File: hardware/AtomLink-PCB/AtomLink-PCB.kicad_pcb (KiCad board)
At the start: 2 copper layers, 21 x 21 mm, 22 parts, among them J1 Conn_01x03, J2 Atom1, J3 Atom2, J4 PF cable, Q1 AS2309, Q2 MUN5235, Q3 AS2309, Q4 MUN5235, U1 LMZM23600V5

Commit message: Schematic & layout changes
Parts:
- added D2: PSM712, Package_TO_SOT_SMD:SOT-23, F.Cu at (47.0, 31.8)
- added Q5: MUN5235, Package_TO_SOT_SMD:SOT-323_SC-70, F.Cu at (45.8, 25.5)
- added R10: ?, Resistor_SMD:R_0402_1005Metric, F.Cu at (45.8, 22.9)
- added R7: 2.2k, Resistor_SMD:R_0805_2012Metric, F.Cu at (49.3, 23.2)
- added R9: 100, Resistor_SMD:R_0402_1005Metric, F.Cu at (45.8, 21.6)
- J4: footprint Connector_PinHeader_2.00mm:PinHeader_1x04_P2.00mm_Vertical -> Connector_PinHeader_1.27mm:PinHeader_1x04_P1.27mm_Vertical
- moved R5 40.8 mm to (62.9, 26.8)
- moved R6 39.6 mm to (61.0, 29.9)
- moved Q2 35.5 mm to (54.5, 33.9)
- moved C2 34.2 mm to (50.4, 34.0)
- moved U1 33.7 mm to (53.1, 19.2), turned to -90 degrees
- moved Q3 33.4 mm to (64.1, 37.4)
- moved R2 33.4 mm to (64.8, 34.5)
- moved R3 33.4 mm to (63.7, 34.5)
- moved R4 33.4 mm to (58.9, 34.6)
- moved R8 33.4 mm to (57.8, 34.6)
- moved D1 32.7 mm to (58.6, 22.3)
- moved C1 32.5 mm to (51.5, 26.6)
- moved Q1 30.9 mm to (55.6, 30.2)
- moved R7 29.1 mm to (53.3, 22.9)
- moved C3 27.0 mm to (48.6, 20.0), turned to 180 degrees
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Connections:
- J1 pad 1: unconnected-(J1-Pad1) -> Net-(J1-Pad1)
- J1 pad 2: unconnected-(J1-Pad2) -> +5V
- J1 pad 3: unconnected-(J1-Pad3) -> GND
- J2 pad 3: G25_ADC -> G25
- J3 pad 1: G33 -> G33_ADC
- Q2 pad 3: G23 -> G21
- Q4 pad 3: G33 -> G25
- R4 pad 2: G25_ADC -> G33_ADC
- R8 pad 1: G25_ADC -> G33_ADC

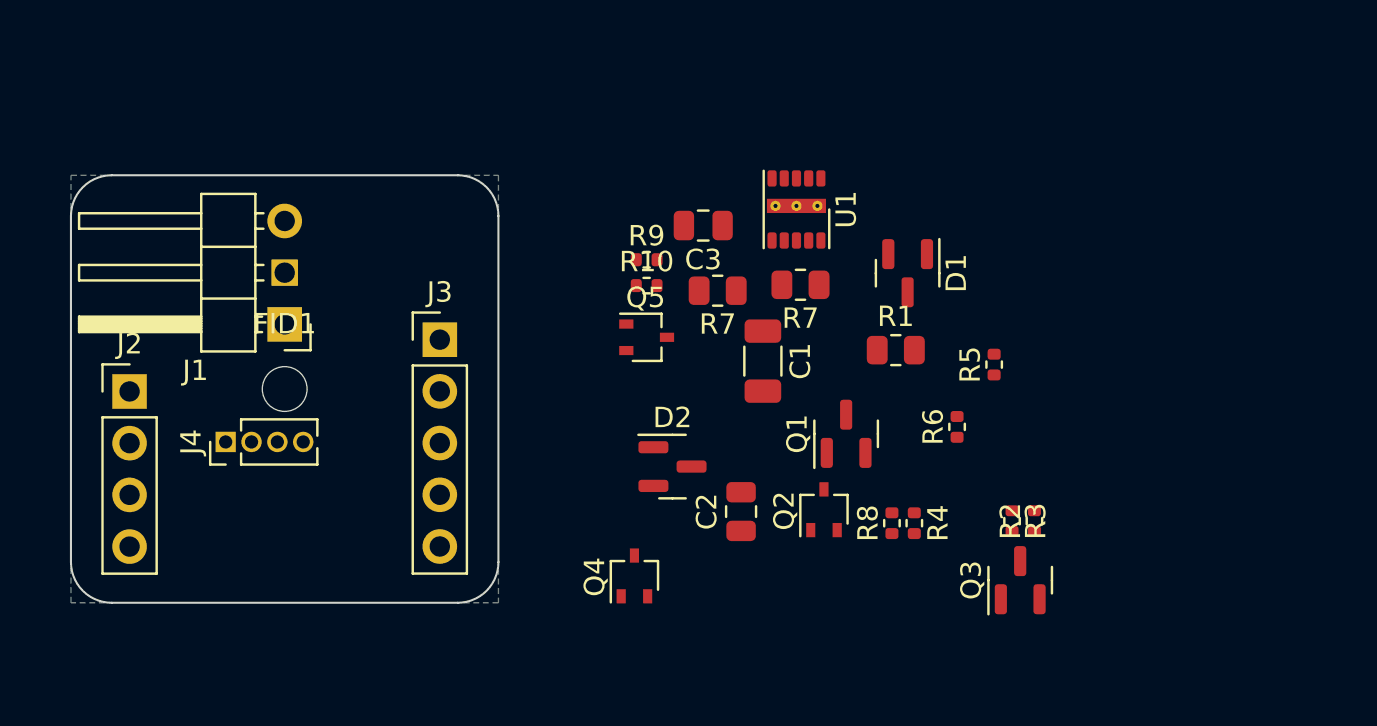
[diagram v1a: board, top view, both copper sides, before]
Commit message: Added Echo variant
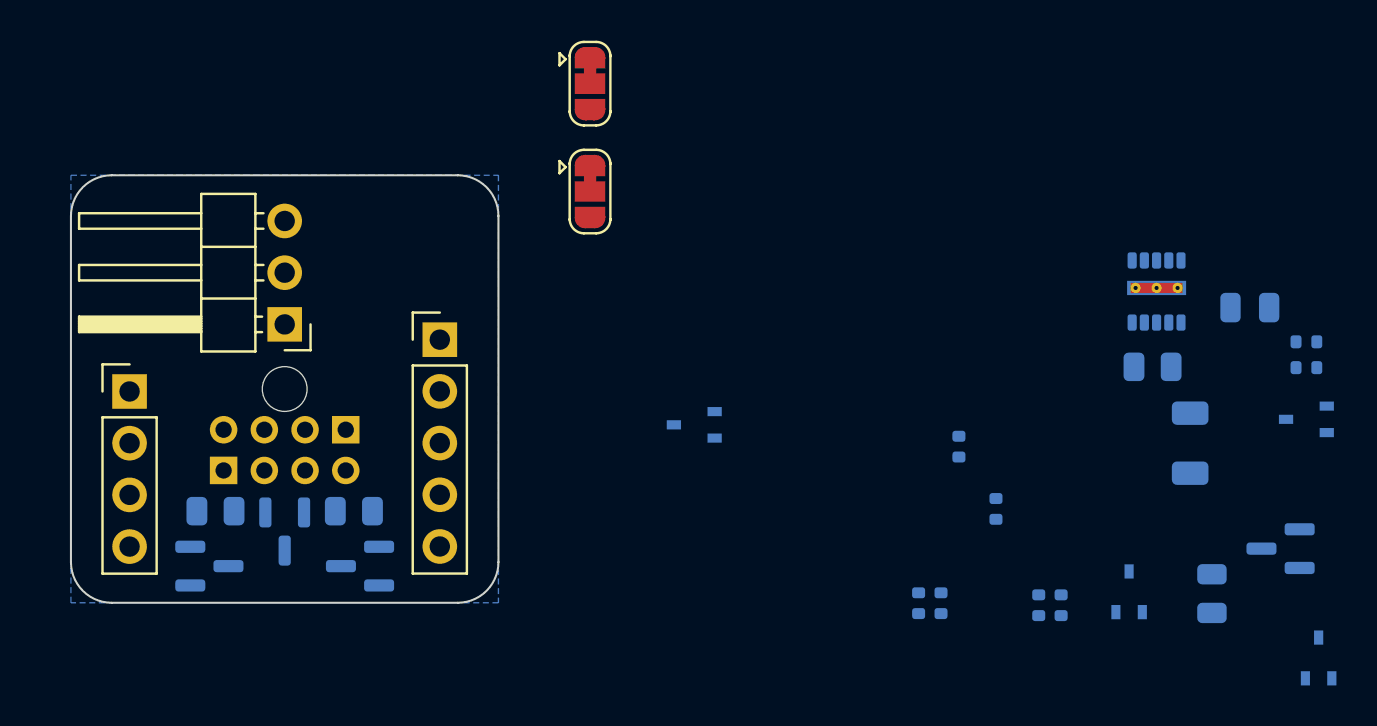
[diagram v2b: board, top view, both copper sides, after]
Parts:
- removed FID1: M2 hole, MountingHole:MountingHole_2.2mm_M2
- added F1: M2, MountingHole:MountingHole_2.2mm_M2, F.Cu at (28.0, 28.0)
- added J5: Grove cable, AtomLink-footprints:PinHeader_1x04_2mm, F.Cu at (28.0, 30.0)
- added JP1: RX switch, Jumper:SolderJumper-3_P1.3mm_Bridged12_RoundedPad1.0x1.5mm, F.Cu at (43.0, 18.3)
- added JP2: TX switch, Jumper:SolderJumper-3_P1.3mm_Bridged12_RoundedPad1.0x1.5mm, F.Cu at (43.0, 13.0)
- added Q6: MUN5235, Package_TO_SOT_SMD:SOT-323_SC-70, B.Cu at (48.1, 29.8)
- C1, C2, C3, D1, D2, Q1, Q2, Q3, Q4, Q5, R1, R2, R3, R4, R5, R6, R7 (x2), R8, R9, U1: moved to B.Cu
- J1: value Conn_01x03 -> Servo/Receiver
- J4: footprint Connector_PinHeader_1.27mm:PinHeader_1x04_P1.27mm_Vertical -> AtomLink-footprints:PinHeader_1x04_2mm
- R10: value ? -> TBD; moved to B.Cu
- moved R1 34.3 mm to (24.6, 34.0), turned to 180 degrees
- moved Q4 33.9 mm to (78.8, 41.2)
- moved D1 33.1 mm to (28.0, 35.0)
- moved Q5 32.7 mm to (78.2, 29.5), turned to 180 degrees
- moved R10 32.7 mm to (78.2, 26.9), turned to 180 degrees
- moved R9 32.7 mm to (78.2, 25.7), turned to 180 degrees
- moved Q3 32.4 mm to (31.7, 36.7), turned to 180 degrees
- moved Q1 31.9 mm to (24.3, 36.7), turned to 0 degrees
- moved D2 30.1 mm to (76.9, 35.8), turned to 180 degrees
- moved C3 27.2 mm to (75.4, 24.0), turned to 0 degrees
- moved C2 23.5 mm to (73.5, 38.0)
- moved C1 21.4 mm to (72.5, 30.7)
- moved R7 20.9 mm to (31.4, 34.0), turned to 0 degrees
- moved U1 18.1 mm to (70.8, 23.2)
- moved R7 17.8 mm to (70.6, 26.9), turned to 0 degrees
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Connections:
- D1 pad 1: PF_M1 -> PF_M2
- D1 pad 2: PF_M2 -> PF_M1
- Q2 pad 3: G21 -> G25
- Q4 pad 3: G25 -> G21
- Q5 pad 1: G19 -> TX
- Q5 pad 3: Net-(D3-Pad1) -> Net-(Q5-Pad3)
- R10 pad 1: +5V -> Net-(Q5-Pad3)
- R10 pad 2: Net-(D3-Pad1) -> GND
- R9 pad 1: Net-(D3-Pad1) -> Net-(Q5-Pad3)
